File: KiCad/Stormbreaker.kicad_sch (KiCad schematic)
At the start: 49 parts, among them J1 Micro_SD_Card_Det2, J2 USB_C_Receptacle_USB2.0_14P, J3 PROG, J5 I2C, Q1 PMOS, Q2 NMOS, SW1 SW_Push, U1 BQ25895RTW, U3 ATtiny1616-M, U4 HUSB238A

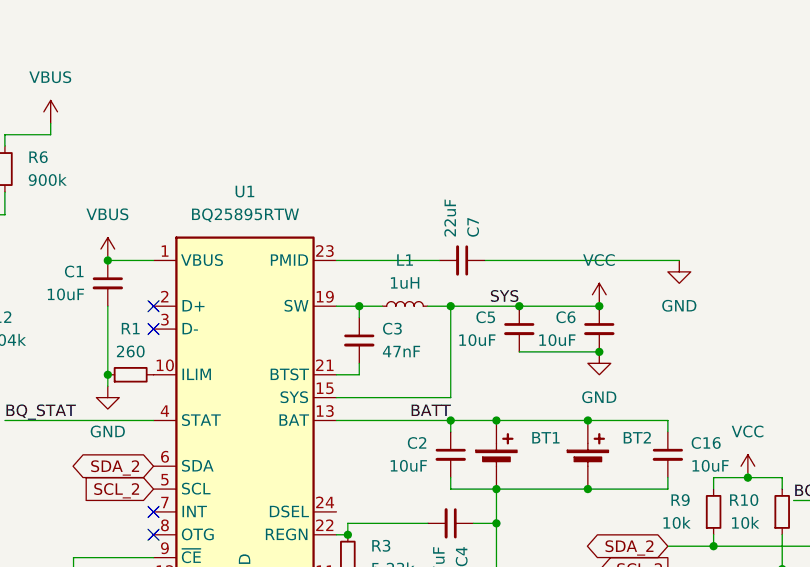
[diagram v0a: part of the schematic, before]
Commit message: Switch to larger inductor
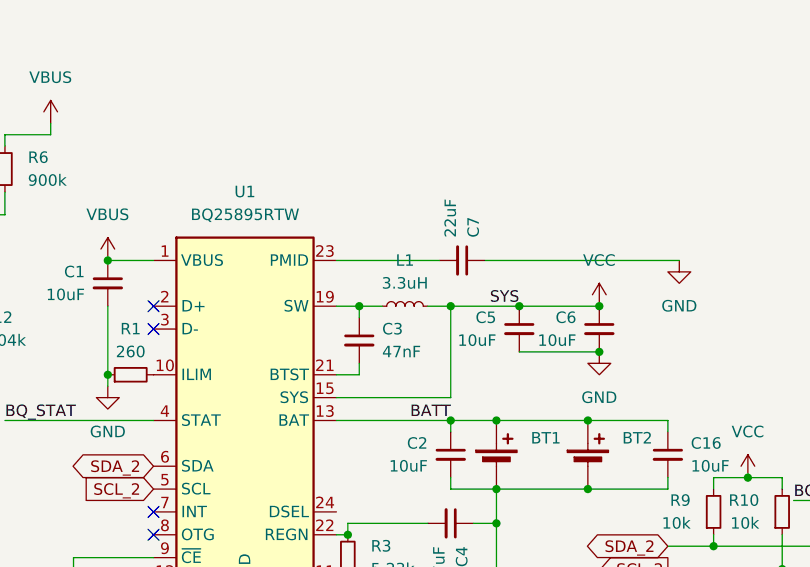
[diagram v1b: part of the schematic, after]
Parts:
- L1: value 1uH -> 3.3uH; footprint Inductor_SMD:L_Taiyo-Yuden_MD-3030 -> Inductor_SMD:L_Chilisin_BMRx00040412
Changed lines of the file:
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@@
 			)
 		)
-		(property "Value" "1uH"
+		(property "Value" "3.3uH"
 			(at 104.14 68.58 90)
 			(effects
@@
 			)
 		)
-		(property "Footprint" "Inductor_SMD:L_Taiyo-Yuden_MD-3030"
+		(property "Footprint" "Inductor_SMD:L_Chilisin_BMRx00040412"
 			(at 104.14 71.12 0)
 			(effects

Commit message: Switch to different button
Something's up with KiCad, not sure why.
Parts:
- SW1: footprint Button_Switch_SMD:Panasonic_EVQPUK_EVQPUB -> Button_Switch_SMD:SW_Push_1P1T-MP_NO_Horizontal_Alps_SKRTLAE010; Mouser https://au.mouser.com/ProductDetail/Panasonic/EVQ-P4KB3Q?qs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 -> https://www.digikey.com.au/en/products/detail/alps-alpine/S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
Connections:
- net GND: now also SW1.MP
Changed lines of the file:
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@@
 			)
 		)
-		(property "Footprint" "Button_Switch_SMD:Panasonic_EVQPUK_EVQPUB"
+		(property "Footprint" "Button_Switch_SMD:SW_Push_1P1T-MP_NO_Horizontal_Alps_SKRTLAE010"
 			(at 224.79 69.85 0)
 			(effects
@@
 			)
 		)
-		(property "Mouser" "https://au.mouser.com/ProductDetail/Panasonic/EVQ-P4KB3Q?qs=0aNVN3t2tDvGc%252BviO4RgAQ%3D%3D"
+		(property "Mouser" "https://www.digikey.com.au/en/products/detail/alps-alpine/SKRTLAE010/19529044?s=N4IgTCBcDaIMoGkBKAVAMgQQKIAYCMOIAugL5A"
 			(at 224.79 74.93 0)
 			(effects
@@
 		(pin "1"
 		)
+		(pin "MP"
+		)
 		(instances

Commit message: Nearing completion of firmware rewrite
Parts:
- L1: footprint Inductor_SMD:L_Chilisin_BMRx00040412 -> Stormbreaker:L_PCMB053T; Digikey (none) -> https://www.digikey.com.au/en/products/detail/susumu/PCMB05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; DigikeyOld https://www.digikey.com.au/en/products/detail/susumu/PCMB05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 -> (none); Mouser https://au.mouser.com/ProductDetail/Wurth-Elektronik/784383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 -> (none); MouserOld https://au.mouser.com/ProductDetail/Vishay-Dale/IHLP2020CZE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 -> (none)
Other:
- moved on the sheet: BT2, C13, C15, C16, Q2, R6, TP4
